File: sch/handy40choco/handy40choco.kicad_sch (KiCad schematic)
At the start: 15 parts, among them J1 Conn_01x02

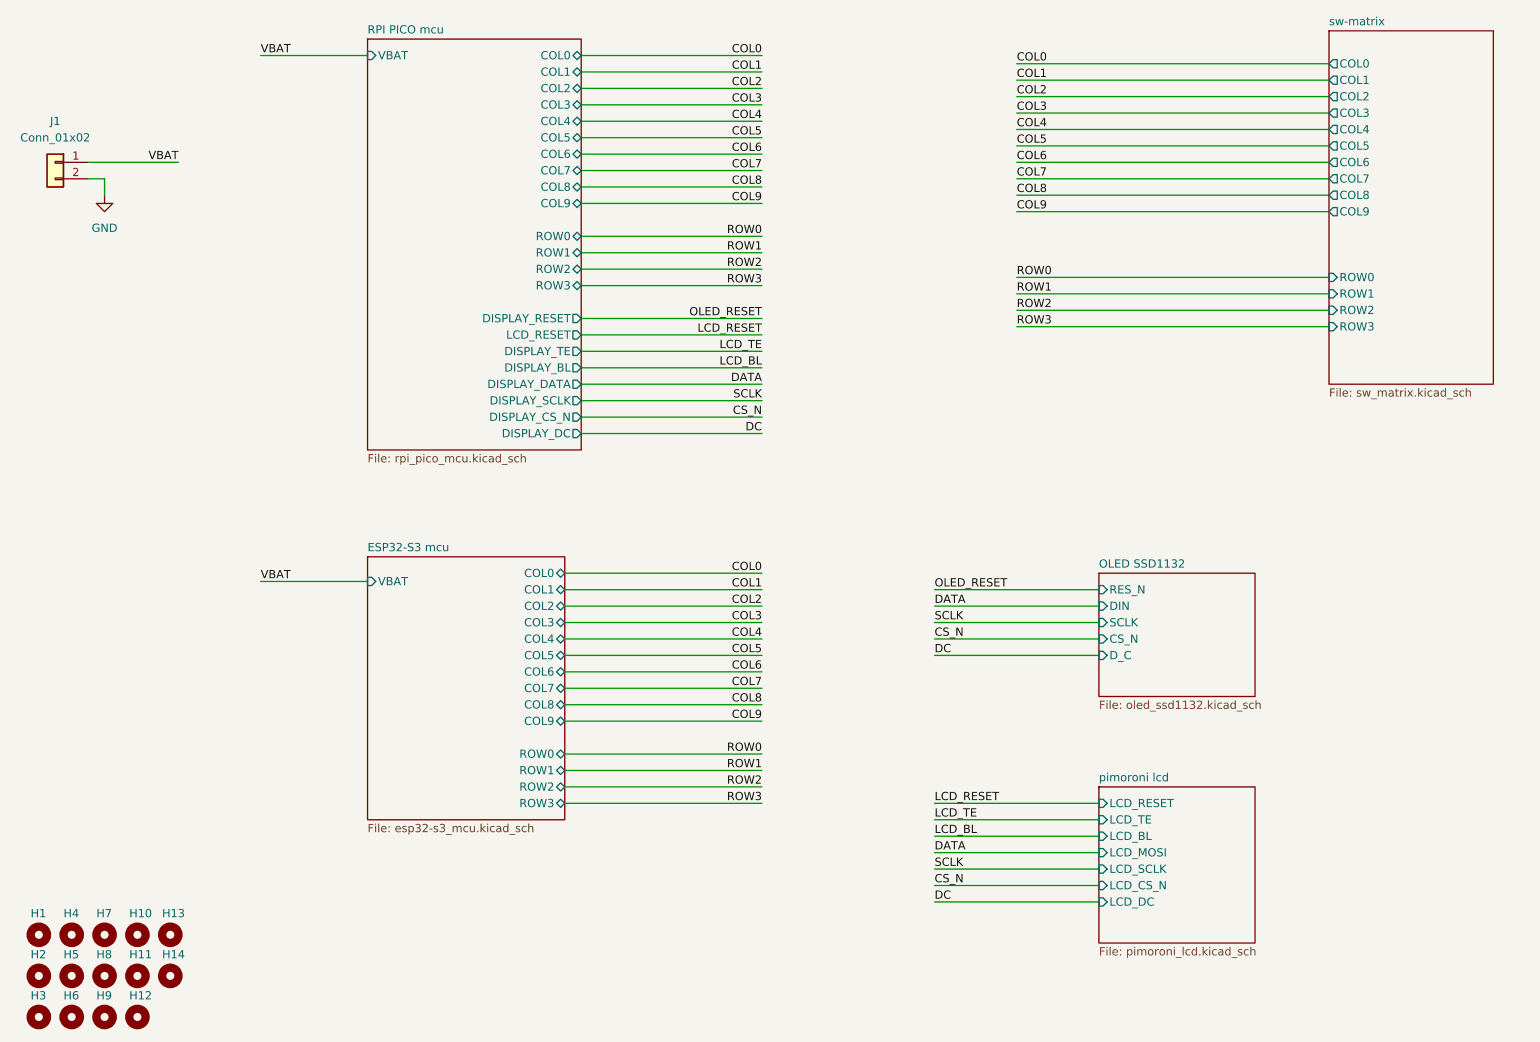
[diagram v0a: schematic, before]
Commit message: Kicad 9に変更しました。 マイコン基板から16ピンのピンヘッダに変更しました。
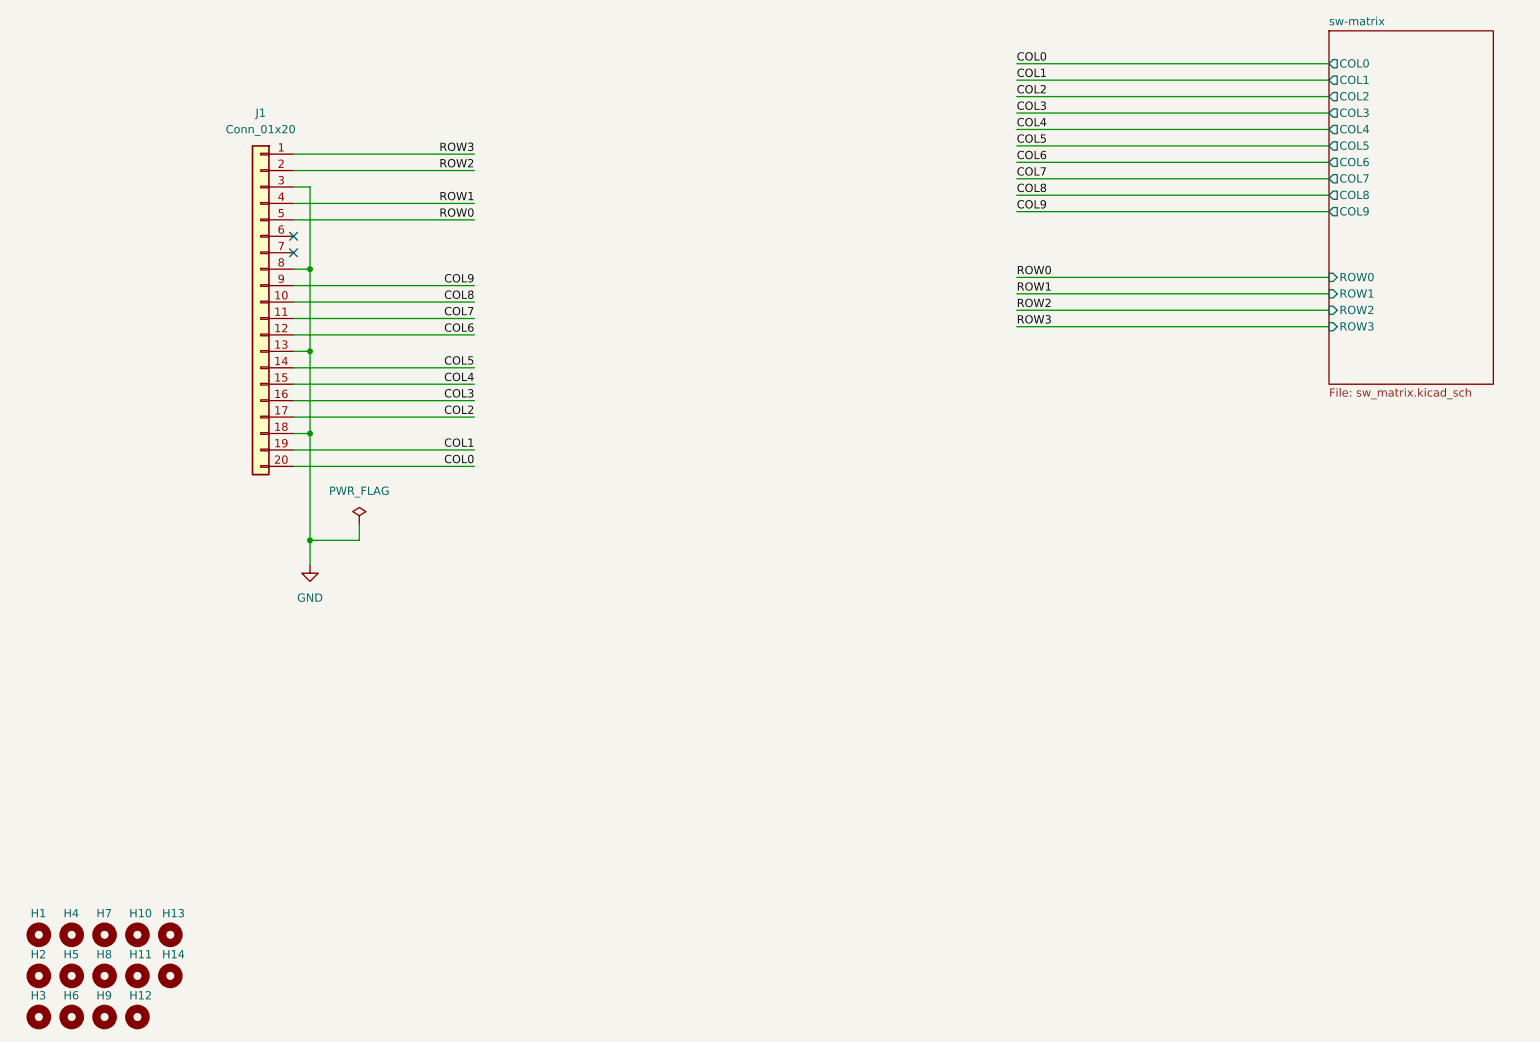
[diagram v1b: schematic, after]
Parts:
- removed J1: Conn_01x02, Connector_JST:JST_PH_B2B-PH-K_1x02_P2.00mm_Vertical, symbol Connector_Generic:Conn_01x02
- added J1: Conn_01x20, Connector_PinHeader_2.54mm:PinHeader_1x20_P2.54mm_Vertical, symbol Connector_Generic:Conn_01x20
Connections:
- net COL0: now also J1.20 (Pin_20)
- net COL1: now also J1.19 (Pin_19)
- net COL2: now also J1.17 (Pin_17)
- net COL3: now also J1.16 (Pin_16)
- net COL4: now also J1.15 (Pin_15)
- net COL5: now also J1.14 (Pin_14)
- net COL6: now also J1.12 (Pin_12)
- net COL7: now also J1.11 (Pin_11)
- net COL8: now also J1.10 (Pin_10)
- net COL9: now also J1.9 (Pin_9)
- net GND: now also J1.13 (Pin_13), J1.18 (Pin_18), J1.3 (Pin_3), J1.8 (Pin_8)
- net ROW0: now also J1.5 (Pin_5)
- net ROW1: now also J1.4 (Pin_4)
- net ROW2: now also J1.2 (Pin_2)
- net ROW3: now also J1.1 (Pin_1)
- no-connect marks 0 -> 2
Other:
- removed sheet ESP32-S3 mcu
- removed sheet OLED SSD1132
- removed sheet RPI PICO mcu
- removed sheet pimoroni lcd

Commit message: ピンヘッダのフットプリントをコンスルーが使えるように、Φ0.85に変更しました。
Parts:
- J1: footprint Connector_PinHeader_2.54mm:PinHeader_1x20_P2.54mm_Vertical -> my_keyswitch:my_PinHeader_1x20_P2.54mm_Vertical_p0.85
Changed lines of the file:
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@@
 			)
 		)
-		(property "Footprint" "Connector_PinHeader_2.54mm:PinHeader_1x20_P2.54mm_Vertical"
+		(property "Footprint" "my_keyswitch:my_PinHeader_1x20_P2.54mm_Vertical_p0.85"
 			(at 58.42 60.96 0)
 			(effects

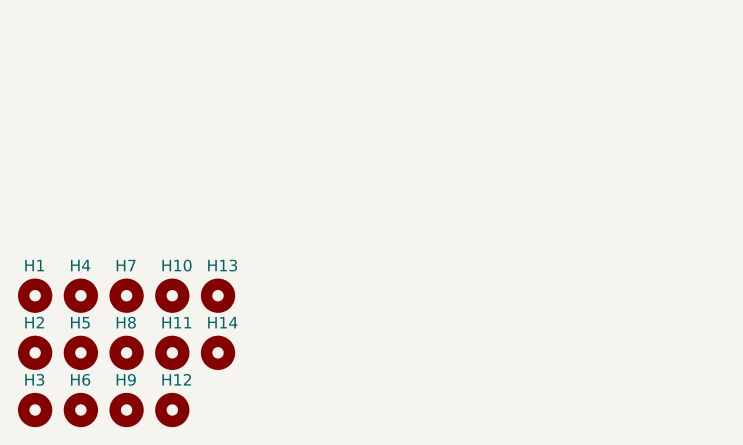
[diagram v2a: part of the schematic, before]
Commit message: マイコンのピンヘッダの位置を基板端から1.27mmに移動しました。 COLの配線を部品面に移動しました。 基板サイズの微調整を行いました。
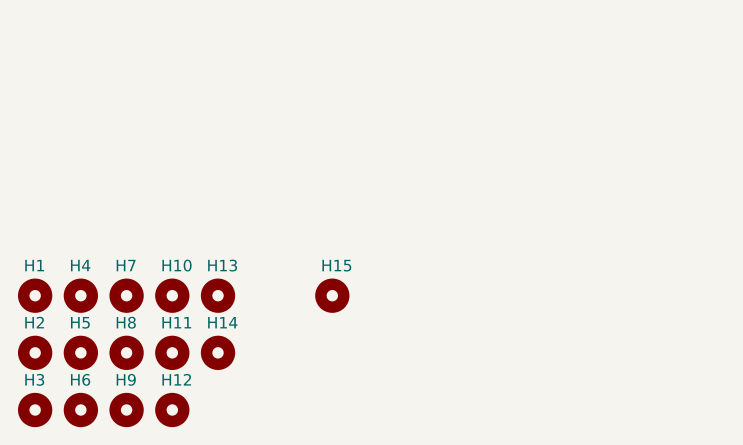
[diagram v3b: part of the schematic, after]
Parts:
- added H15: MountingHole, my_keyswitch:my_MountingHole_2.2mm_M2, symbol Mechanical:MountingHole
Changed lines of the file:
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@@
+	)
+	(symbol
+		(lib_id "Mechanical:MountingHole")
+		(at 57.15 158.75 0)
+		(unit 1)
+		(exclude_from_sim yes)
+		(in_bom no)
+		(on_board yes)
+		(dnp no)
+		(property "Reference" "H15"
+			(at 55.88 155.448 0)
+			(effects
+				(font
+					(size 1.27 1.27)
+				)
+				(justify left)
+			)
+		)
+		(property "Value" "MountingHole"
+			(at 59.69 160.0199 0)
+			(effects
+				(font
+					(size 1.27 1.27)
+				)
+				(justify left)
+				(hide yes)
+			)
+		)
+		(property "Footprint" "my_keyswitch:my_MountingHole_2.2mm_M2"
+			(at 57.15 158.75 0)
+			(effects
+				(font
+					(size 1.27 1.27)
+				)
+				(hide yes)
+			)
+		)
+		(property "Datasheet" "~"
+			(at 57.15 158.75 0)
+			(effects
+				(font
+					(size 1.27 1.27)
+				)
+				(hide yes)
+			)
+		)
+		(property "Description" "Mounting Hole without connection"
+			(at 57.15 158.75 0)
+			(effects
+				(font
+					(size 1.27 1.27)
+				)
+				(hide yes)
+			)
+		)
+		(instances
+			(project "handy40choco"
+				(path "/c7705321-b11d-4074-930b-69ce3166659a"
+					(reference "H15")
+					(unit 1)
+				)
+			)
+		)
 	)
 	(symbol
